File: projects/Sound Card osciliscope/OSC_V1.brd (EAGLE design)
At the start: 29.2 x 58.1 mm, 11 parts, among them X1 22-23-2021, X2 22-23-2021

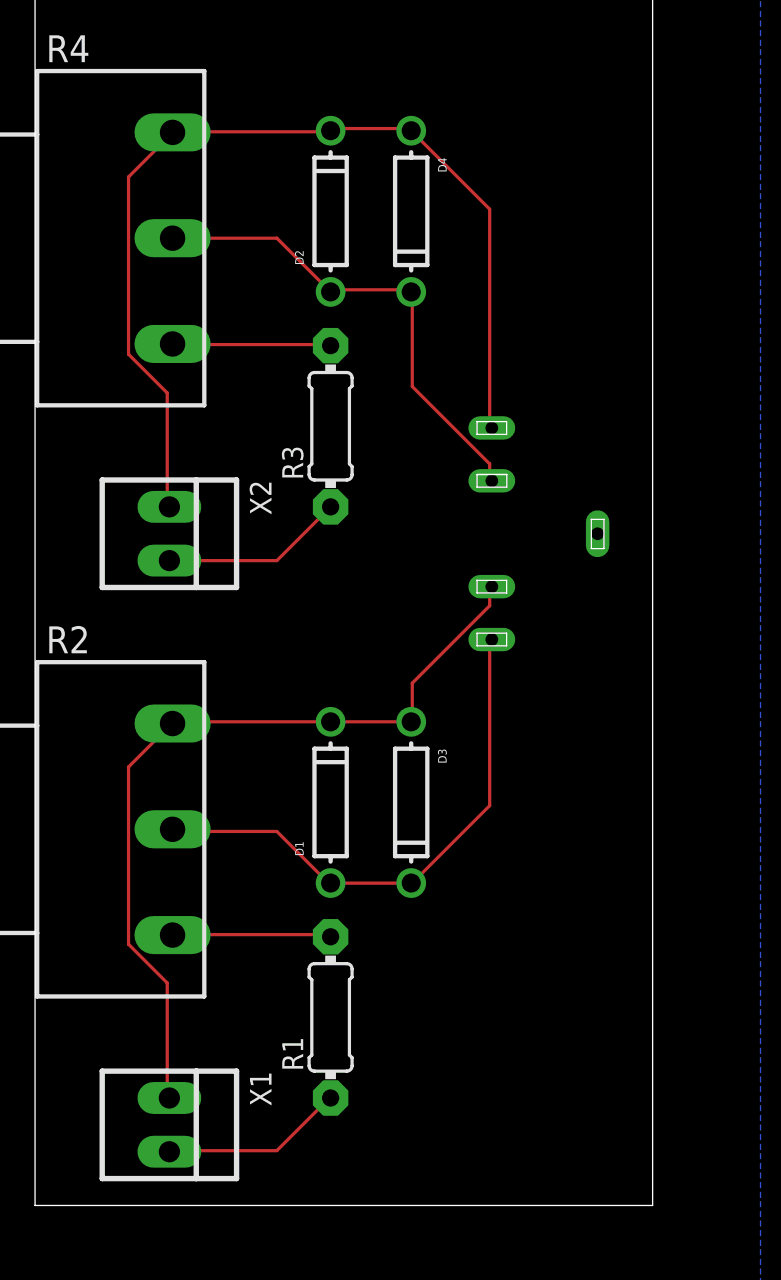
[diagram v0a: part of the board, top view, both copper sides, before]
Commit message: Update Library and Sccope
Added 3pin Jack to Library and finished up with the osciliscope
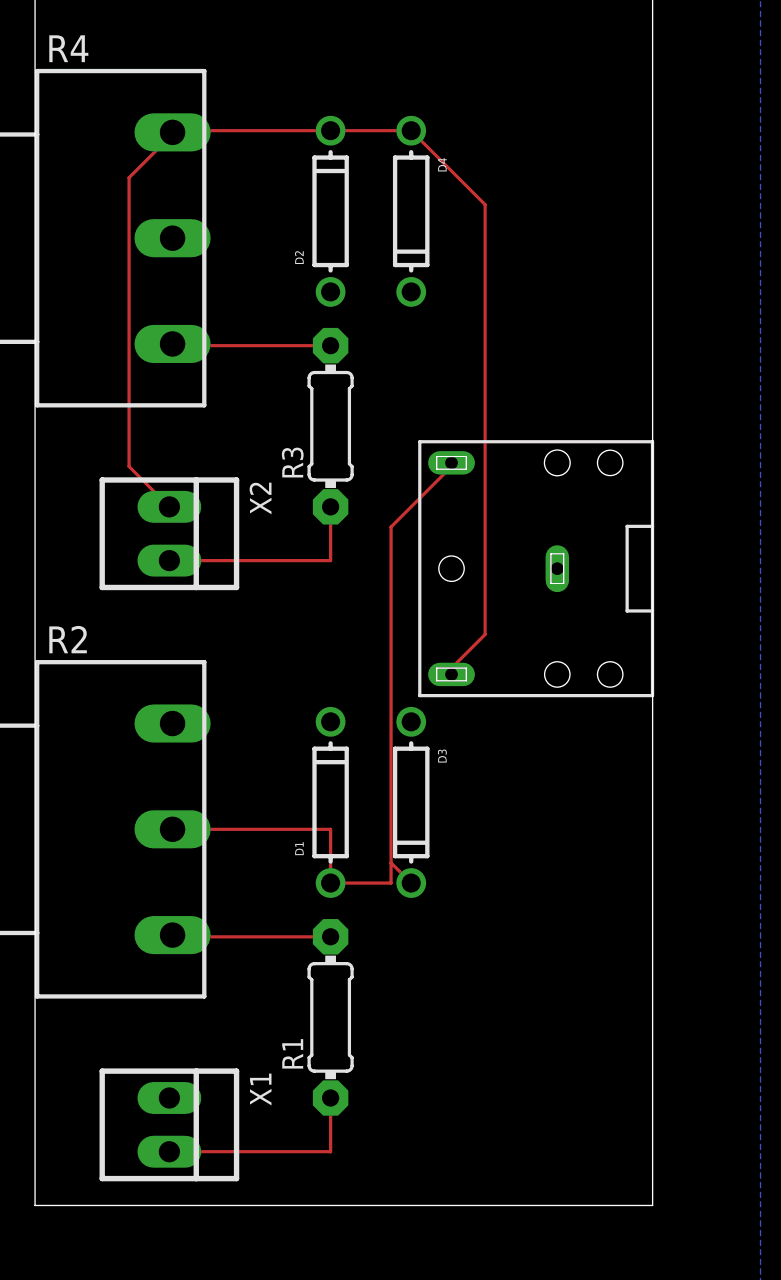
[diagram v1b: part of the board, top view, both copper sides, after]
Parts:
- U$1: value AUDIO5PIN -> AUDIO3PIN; device Test:AUDIO5PIN -> Test:AUDIO3PIN
- moved U$1 2.52 mm to (19.7, 30.1)
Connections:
- removed net N$7: D2.A, D4.C, R4.1S, U$1.A3
- net GND: now also D2.A, D4.C, R4.1S; no longer U$1.A2
- net N$3: now also U$1.INPUT2; no longer U$1.A1
- net N$8: now also U$1.INPUT1; no longer U$1.A4
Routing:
- net GND: track 38.7 -> 0.00 mm
- net N$7: track 23.0 -> 0.00 mm
- net N$8: track 46.4 -> 58.4 mm
- net N$3: track 25.5 -> 35.3 mm
- net N$1: track 8.66 -> 10.2 mm
- net N$5: track 8.67 -> 10.2 mm

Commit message: Updated board
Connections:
- net GND: now also D2.C, D4.A, R4.1A, X2.1; no longer D2.A, D4.C, R4.1S
- net N$8: now also D2.A, D4.C, R4.1S; no longer D2.C, D4.A, R4.1A, X2.1
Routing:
- net N$8: track 58.4 -> 34.0 mm
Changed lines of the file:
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@@
 <vertex x="-6.35" y="63.5"/>
 </polygon>
+<contactref element="U$1" pad="GND"/>
 <contactref element="X1" pad="1"/>
 <contactref element="R2" pad="1A"/>
 <contactref element="D1" pad="C"/>
 <contactref element="D3" pad="A"/>
-<contactref element="R4" pad="1S"/>
-<contactref element="D2" pad="A"/>
-<contactref element="D4" pad="C"/>
-<contactref element="U$1" pad="GND"/>
+<contactref element="X2" pad="1"/>
+<contactref element="R4" pad="1A"/>
+<contactref element="D4" pad="A"/>
+<contactref element="D2" pad="C"/>
 </signal>
 <signal name="N$1">
@@
 <wire x1="6.6675" y1="12.7" x2="6.5" y2="12.78" width="0.1524" layer="1"/>
 </signal>
-<signal name="N$3">
+<signal name="N$4">
 <contactref element="R2" pad="1S"/>
+<contactref element="U$1" pad="INPUT2"/>
 <contactref element="D1" pad="A"/>
 <contactref element="D3" pad="C"/>
-<contactref element="U$1" pad="INPUT2"/>
 <wire x1="16.8275" y1="32.0675" x2="19.685" y2="34.925" width="0.1524" layer="1"/>
 <wire x1="16.8275" y1="16.1925" x2="16.8275" y2="32.0675" width="0.1524" layer="1"/>
@@
 </signal>
 <signal name="N$8">
-<contactref element="R4" pad="1A"/>
-<contactref element="D4" pad="A"/>
-<contactref element="D2" pad="C"/>
-<contactref element="X2" pad="1"/>
+<contactref element="R4" pad="1S"/>
 <contactref element="U$1" pad="INPUT1"/>
-<wire x1="4.445" y1="34.925" x2="6.35" y2="33.02" width="0.1524" layer="1"/>
-<wire x1="4.445" y1="48.5775" x2="4.445" y2="34.925" width="0.1524" layer="1"/>
-<wire x1="6.35" y1="50.4825" x2="4.445" y2="48.5775" width="0.1524" layer="1"/>
-<wire x1="6.35" y1="50.4825" x2="6.5" y2="50.72" width="0.1524" layer="1"/>
+<contactref element="D4" pad="C"/>
+<contactref element="D2" pad="A"/>
 <wire x1="21.2725" y1="26.9875" x2="19.685" y2="25.4" width="0.1524" layer="1"/>
-<wire x1="21.2725" y1="47.3075" x2="21.2725" y2="26.9875" width="0.1524" layer="1"/>
-<wire x1="17.78" y1="50.8" x2="21.2725" y2="47.3075" width="0.1524" layer="1"/>
+<wire x1="21.2725" y1="39.6875" x2="21.2725" y2="26.9875" width="0.1524" layer="1"/>
+<wire x1="17.78" y1="43.18" x2="21.2725" y2="39.6875" width="0.1524" layer="1"/>
 <wire x1="19.685" y1="25.4" x2="19.685" y2="25.099" width="0.1524" layer="1"/>
-<wire x1="17.78" y1="50.8" x2="13.97" y2="50.8" width="0.1524" layer="1"/>
-<wire x1="13.97" y1="50.8" x2="6.6675" y2="50.8" width="0.1524" layer="1"/>
-<wire x1="6.6675" y1="50.8" x2="6.5" y2="50.72" width="0.1524" layer="1"/>
+<wire x1="17.78" y1="43.18" x2="13.97" y2="43.18" width="0.1524" layer="1"/>
+<wire x1="13.97" y1="45.72" x2="6.5" y2="45.72" width="0.1524" layer="1"/>
+<wire x1="13.97" y1="43.18" x2="13.97" y2="45.72" width="0.1524" layer="1"/>
 </signal>
 </signals>
